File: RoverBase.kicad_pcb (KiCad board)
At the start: 2 copper layers, 90 x 118 mm, 64 parts, among them J1 Conn_01x01, J2 Conn_01x06, J3 Conn_01x04, J4 Conn_01x02, J5 Conn_01x03, J6 Conn_02x03_Counter_Clockwise, J7 Conn_02x03_Counter_Clockwise, J8 Conn_01x01, J9 Conn_01x06, SW1 SW_SPDT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

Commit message: Remove diodes and add thermal via for motor controllers
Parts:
- removed D4, D5: D_Schottky, Diode_SMD:D_SOD-323
- C1: value 1.0uF-50V -> 1.0uF, 50V
- U2: value ACS711xLCTR-12AB -> ACS711ELCTR-12AB-T
- U5, U6: footprint Package_SON:WSON-8-1EP_2x2mm_P0.5mm_EP0.9x1.6mm -> Package_SON:WSON-8-1EP_2x2mm_P0.5mm_EP0.9x1.6mm_ThermalVias
- moved C18 4.06 mm to (156.6, 40.3)
- moved C20 3.80 mm to (153.3, 40.8), turned to 270 degrees
- moved C19 1.33 mm to (158.1, 135.8), turned to 270 degrees
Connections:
- C19 pad 1: /VIN -> /FC_5V
- C20 pad 2: /VIN -> /FC_5V
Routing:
- net GND: track 89.2 -> 83.4 mm, vias 25 -> 24
- net Net-(J7-Pad2): track 12.5 -> 13.1 mm
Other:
- outline, holes or cut-outs redrawn

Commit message: RoHS Compliance
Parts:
- added REF**: RoHS-Logo_6mm_SilkScreen, Symbol:RoHS-Logo_6mm_SilkScreen, B.Cu at (223.6, 123.0)

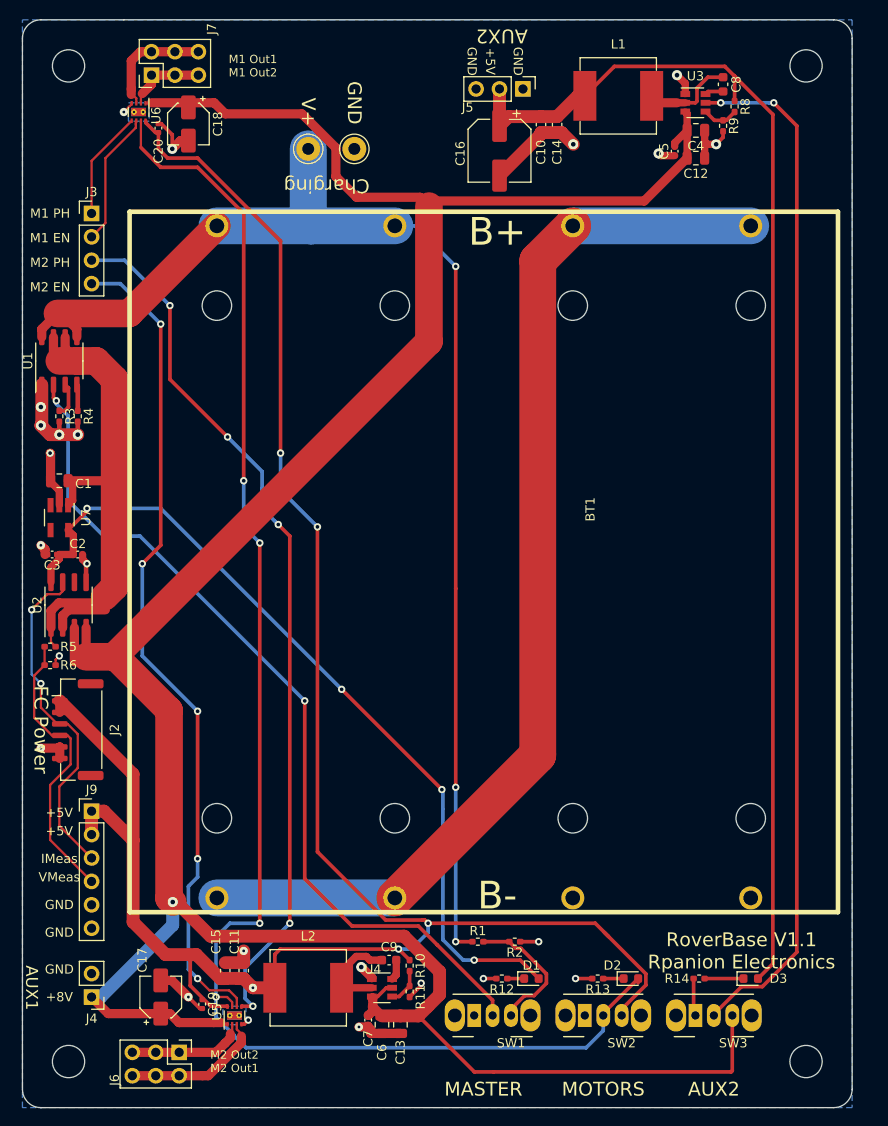
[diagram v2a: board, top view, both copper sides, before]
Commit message: Using FET and fuse instead of switch
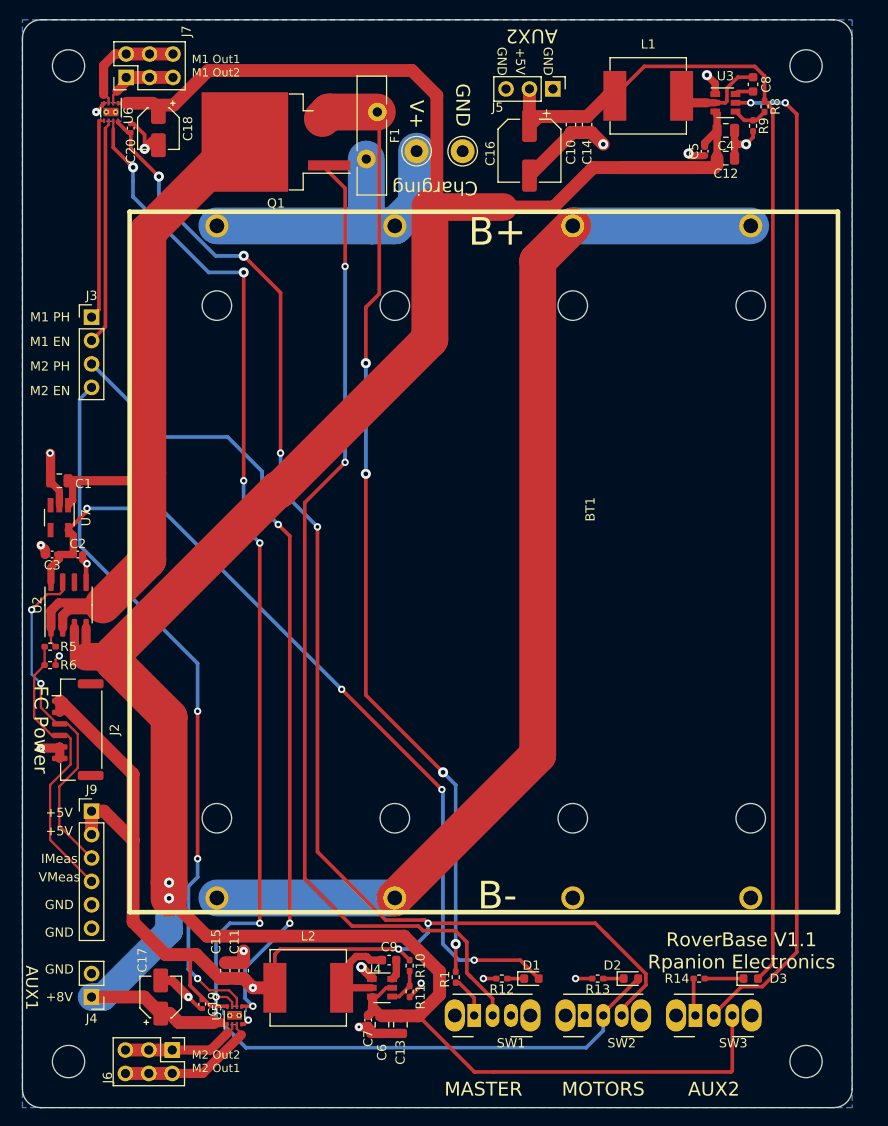
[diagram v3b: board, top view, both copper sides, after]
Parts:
- removed R2, R4: 10k, Resistor_SMD:R_0402_1005Metric_Pad0.72x0.64mm_HandSolder
- removed R3: 1k, Resistor_SMD:R_0402_1005Metric_Pad0.72x0.64mm_HandSolder
- removed U1: VN5E160MS-E, Package_SO:SO-8_3.9x4.9mm_P1.27mm
- added F1: Polyfuse, Fuse:Fuse_Bourns_MF-RG800, F.Cu at (177.1, 39.0)
- added Q1: MOSFET P-CH 40V 50A, Package_TO_SOT_SMD:TO-263-2, F.Cu at (166.1, 42.2)
- R1: value 10k -> 1k
- moved J1 11.8 mm to (186.3, 43.2)
- moved J8 11.8 mm to (181.3, 43.2)
- moved J3 11.2 mm to (146.1, 61.2)
- moved REF** 8.80 mm to (223.6, 114.2), turned to 90 degrees
- moved R1 4.54 mm to (185.6, 132.8), turned to 90 degrees
- moved C18 3.29 mm to (153.3, 40.8)
- moved C10 3.25 mm to (198.1, 40.4)
- moved C12 3.25 mm to (214.9, 44.0)
- moved C14 3.25 mm to (199.8, 40.4)
- moved C16 3.25 mm to (193.6, 43.2)
- moved C4 3.25 mm to (214.9, 41.0)
- moved C5 3.25 mm to (212.6, 43.2)
- moved C8 3.25 mm to (217.8, 36.0)
- moved J5 3.25 mm to (196.1, 36.5)
- moved L1 3.25 mm to (206.5, 37.2)
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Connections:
- R1 pad 1: Net-(BT1-Pad3) -> Net-(R1-Pad1)
- R1 pad 2: Net-(R1-Pad2) -> Net-(F1-Pad1)
- SW1 pad 1: GND -> Net-(R1-Pad1)
- SW1 pad 3: Net-(R1-Pad2) -> GND
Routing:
- net Net-(F1-Pad1): track 0.00 -> 104.4 mm, vias 0 -> 4
- net Net-(BT1-Pad3): track 139.5 -> 38.1 mm, vias 3 -> 0
- net /VIN: track 299.8 -> 333.8 mm, vias 1 -> 2
- net Net-(C1-Pad1): track 61.7 -> 85.1 mm
- net Net-(R1-Pad2): track 15.0 -> 0.00 mm
- net Net-(Q1-Pad1): track 95.9 -> 110.0 mm
- net Net-(J3-Pad4): track 90.5 -> 76.9 mm, vias 5 -> 3
- net GND: track 83.4 -> 69.9 mm, vias 24 -> 19
- net Net-(J3-Pad1): track 11.9 -> 22.2 mm
- net Net-(J3-Pad2): track 14.6 -> 24.6 mm
- net Net-(J3-Pad3): track 95.5 -> 86.2 mm, vias 5 -> 3
- net Net-(R1-Pad1): track 0.00 -> 4.59 mm
- net Net-(C10-Pad1): track 137.9 -> 133.8 mm
- net Net-(R3-Pad1): track 3.74 -> 0.00 mm
- net Net-(D2-Pad2): track 163.1 -> 166.4 mm, vias 4 -> 6
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
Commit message: Minor PCB updates
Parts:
- moved C18 0.40 mm to (153.4, 40.4)
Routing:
- net /VIN: track 333.8 -> 334.7 mm, vias 2 -> 3
- net Net-(J6-Pad1): track 12.7 -> 13.3 mm
- net /FC_5V: vias 7 -> 6

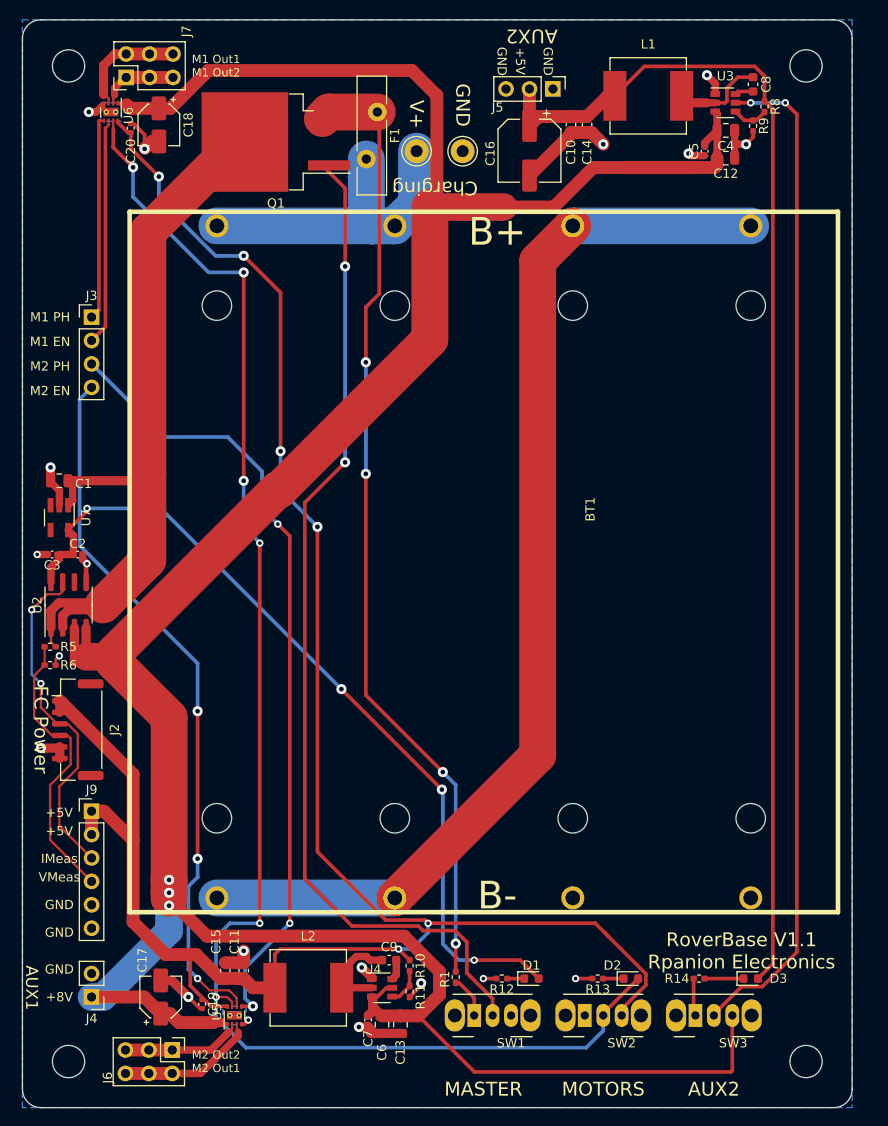
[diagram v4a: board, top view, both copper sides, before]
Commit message: Upgrade to KiCad6
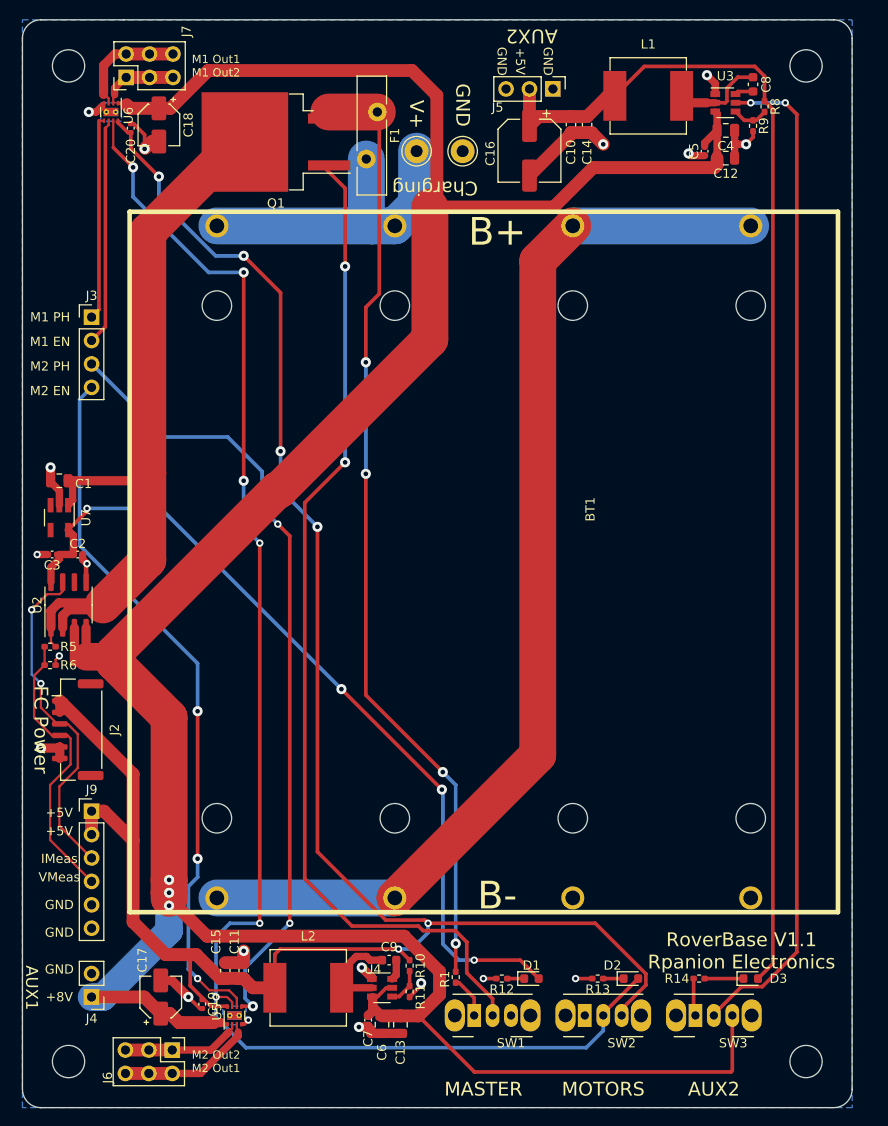
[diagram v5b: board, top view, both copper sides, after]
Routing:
- net /VIN: track 334.7 -> 317.2 mm
- net Net-(D2-Pad2): track 166.4 -> 164.0 mm
- net Net-(C10-Pad1): track 133.8 -> 131.5 mm
- net Net-(BT1-Pad3): track 38.1 -> 35.9 mm
- net Net-(F1-Pad1): track 104.4 -> 103.1 mm
- net Net-(J2-Pad3): track 38.4 -> 37.1 mm
- net Net-(C1-Pad1): track 85.1 -> 84.2 mm
- net /FC_5V: track 225.4 -> 224.6 mm
- net GND: track 69.6 -> 68.9 mm
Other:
- net class Default removed
